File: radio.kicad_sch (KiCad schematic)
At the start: 28 parts, among them IC5 S2-LPQTR, IC6 BALF-SPI2-01D3, Y3 Crystal_GND24

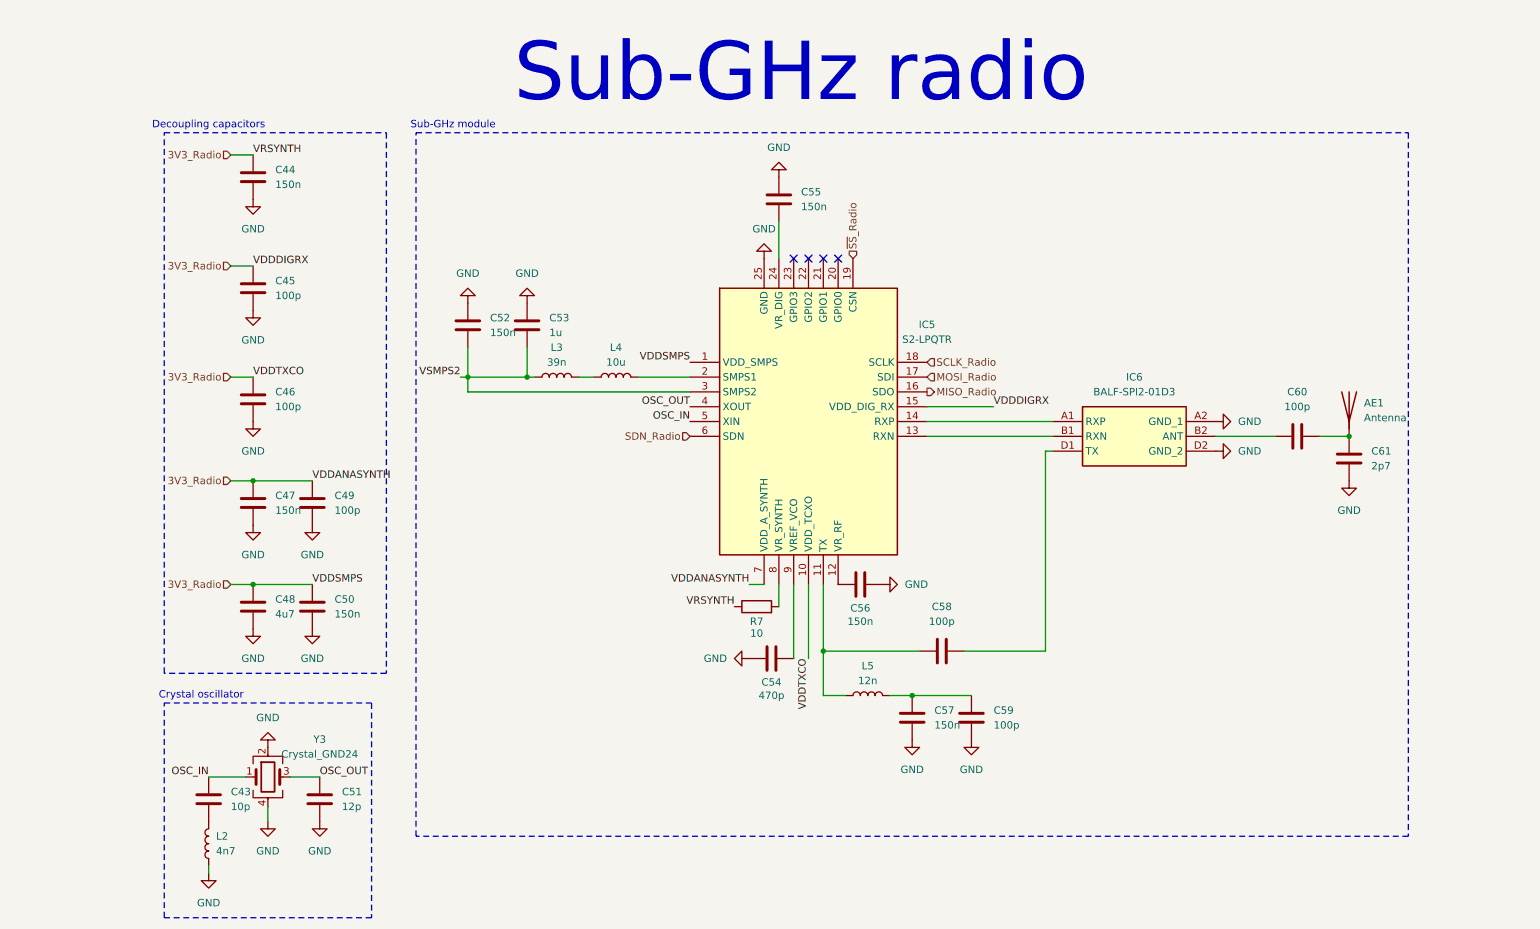
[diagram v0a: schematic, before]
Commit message: Setup crystal oscillators for MCU and S2LP
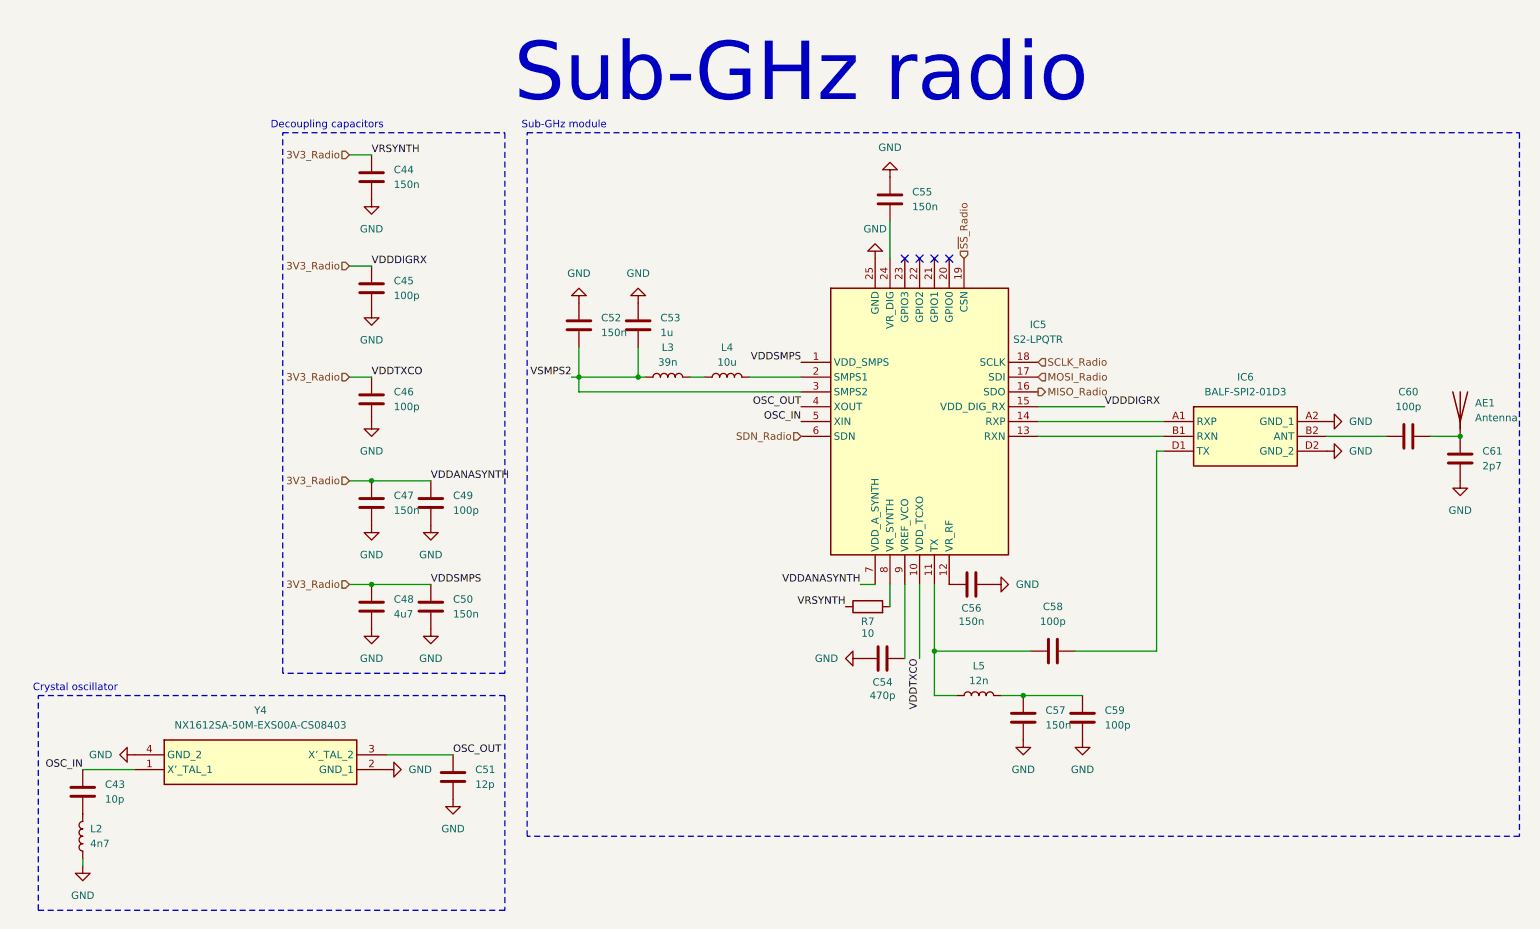
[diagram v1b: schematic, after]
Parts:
- removed Y3: Crystal_GND24, symbol Device:Crystal_GND24
- added Y4: NX1612SA-50M-EXS00A-CS08403, weather-station-poc-fp:NX1612SA50MEXS00ACS08403, symbol weather-station-poc-sym:NX1612SA-50M-EXS00A-CS08403
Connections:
- net GND: now also Y4.2 (GND_1), Y4.4 (GND_2)
- net OSC_IN: now also Y4.1 (X’_TAL_1)
- net OSC_OUT: now also Y4.3 (X’_TAL_2)
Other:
- moved on the sheet: AE1, C43, C44, C45, C46, C47, C48, C49, C50, C51, C52, C53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

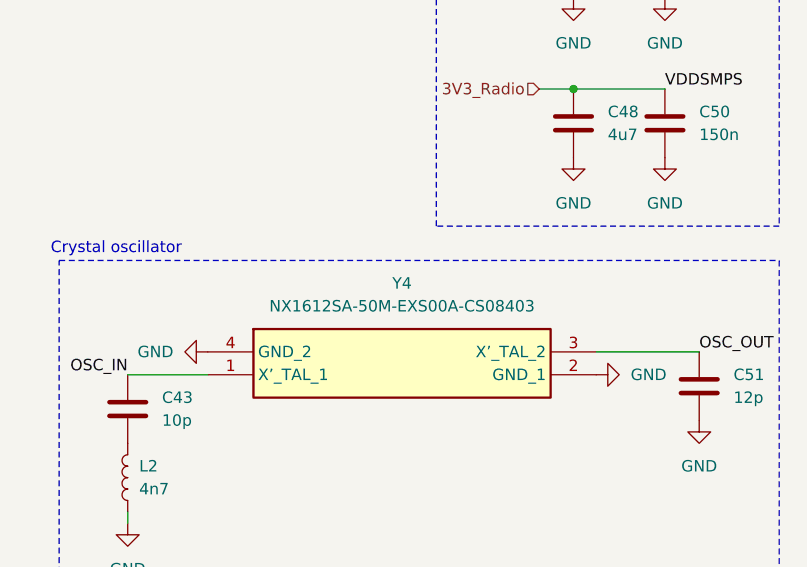
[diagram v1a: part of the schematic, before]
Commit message: Use preconised diodes for USB-C by ST
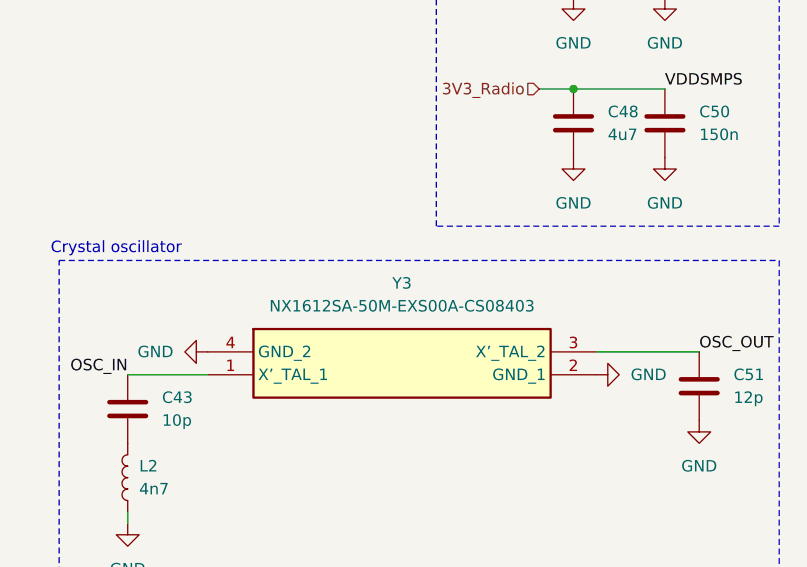
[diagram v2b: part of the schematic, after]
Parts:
- renumbered Y4 to Y3
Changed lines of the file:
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@@
 		(dnp no)
 		(fields_autoplaced yes)
-		(property "Reference" "#PWR077"
+		(property "Reference" "#PWR072"
 			(at 27.94 142.24 0)
 			(effects
@@
 			(project "weather-station-poc"
 				(path "/38eb53bb-294e-46e4-ad59-fd355ca373b9/31741ecc-719f-4191-b75e-d75152dfd251"
-					(reference "#PWR077")
+					(reference "#PWR072")
 					(unit 1)
 				)
@@
 		(dnp no)
 		(fields_autoplaced yes)
-		(property "Reference" "#PWR073"
+		(property "Reference" "#PWR074"
 			(at 74.93 72.39 0)
 			(effects
@@
 			(project "weather-station-poc"
 				(path "/38eb53bb-294e-46e4-ad59-fd355ca373b9/31741ecc-719f-4191-b75e-d75152dfd251"
-					(reference "#PWR073")
+					(reference "#PWR074")
 					(unit 1)
 				)
@@
 		(dnp no)
 		(fields_autoplaced yes)
-		(property "Reference" "Y4"
+		(property "Reference" "Y3"
 			(at 55.88 134.62 0)
 			(effects
@@
 			(project ""
 				(path "/38eb53bb-294e-46e4-ad59-fd355ca373b9/31741ecc-719f-4191-b75e-d75152dfd251"
-					(reference "Y4")
+					(reference "Y3")
 					(unit 1)
 				)
@@
 		(dnp no)
 		(fields_autoplaced yes)
-		(property "Reference" "#PWR075"
+		(property "Reference" "#PWR076"
 			(at 74.93 109.22 0)
 			(effects
@@
 			(project "weather-station-poc"
 				(path "/38eb53bb-294e-46e4-ad59-fd355ca373b9/31741ecc-719f-4191-b75e-d75152dfd251"
-					(reference "#PWR075")
+					(reference "#PWR076")
 					(unit 1)
 				)
@@
 		(dnp no)
 		(fields_autoplaced yes)
-		(property "Reference" "#PWR072"
+		(property "Reference" "#PWR073"
 			(at 74.93 53.34 0)
 			(effects
@@
 			(project "weather-station-poc"
 				(path "/38eb53bb-294e-46e4-ad59-fd355ca373b9/31741ecc-719f-4191-b75e-d75152dfd251"
-					(reference "#PWR072")
+					(reference "#PWR073")
 					(unit 1)
 				)
@@
 		(dnp no)
 		(fields_autoplaced yes)
-		(property "Reference" "#PWR076"
+		(property "Reference" "#PWR077"
 			(at 74.93 127 0)
 			(effects
@@
 			(project ""
 				(path "/38eb53bb-294e-46e4-ad59-fd355ca373b9/31741ecc-719f-4191-b75e-d75152dfd251"
-					(reference "#PWR076")
+					(reference "#PWR077")
 					(unit 1)
 				)
@@
 		(dnp no)
 		(fields_autoplaced yes)
-		(property "Reference" "#PWR074"
+		(property "Reference" "#PWR075"
 			(at 74.93 91.44 0)
 			(effects
@@
 			(project "weather-station-poc"
 				(path "/38eb53bb-294e-46e4-ad59-fd355ca373b9/31741ecc-719f-4191-b75e-d75152dfd251"
-					(reference "#PWR074")
+					(reference "#PWR075")
 					(unit 1)
 				)

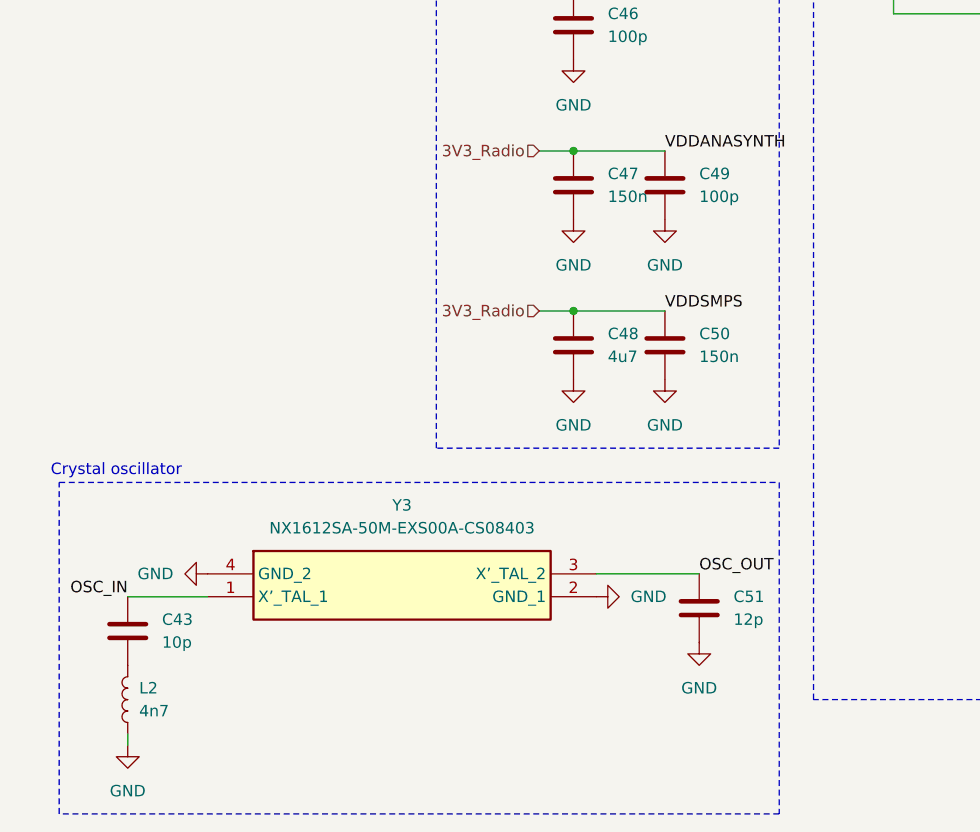
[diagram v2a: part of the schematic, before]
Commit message: Homogenation of symbols
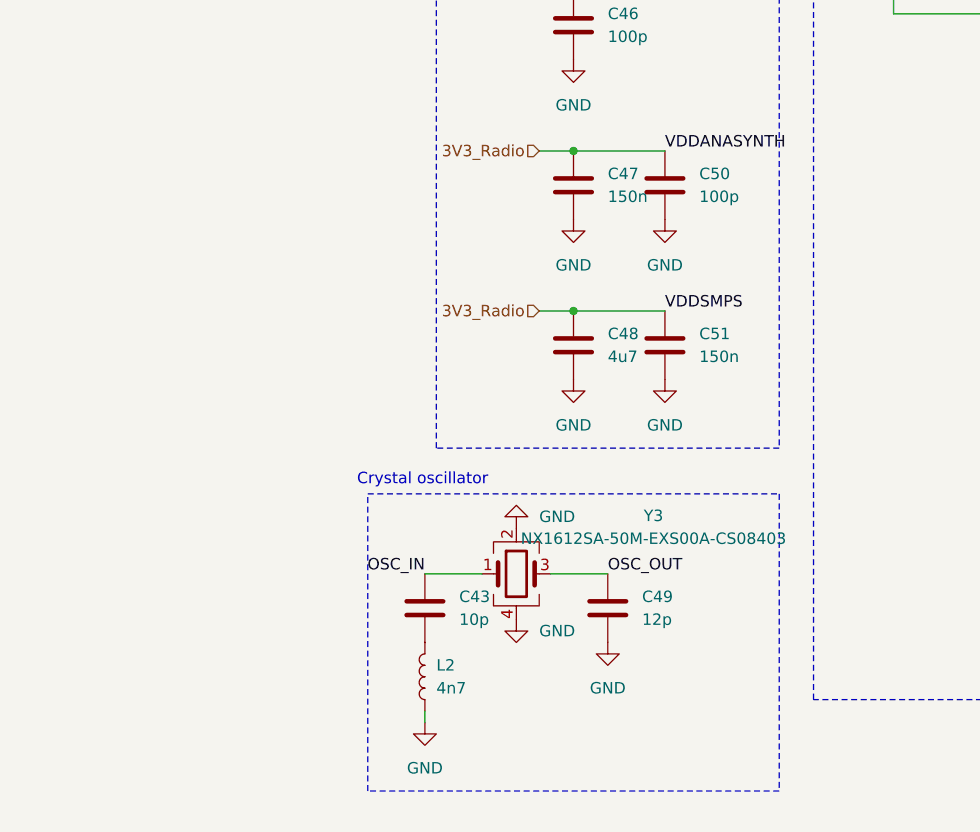
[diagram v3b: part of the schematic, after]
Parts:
- Y3: symbol weather-station-poc-sym:NX1612SA-50M-EXS00A-CS08403 -> Device:Crystal_GND24
- renumbered C51 to C49, C49 to C50, C50 to C51
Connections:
- net OSC_IN: now also C43.1; no longer C43.2
- net at L2.2: now also C43.2; no longer C43.1
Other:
- moved on the sheet: C43, C49, L2

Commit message: Fill the cartridge for all schematics
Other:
- company: (none) -> Julien Cruvieux
- title: (none) -> Radio Sub-GHz
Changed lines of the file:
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@@
 	(paper "A4")
 	(title_block
-		(date "2025-11-01")
+		(title "Radio Sub-GHz")
+		(date "2025-12-26")
+		(rev "A")
+		(company "Julien Cruvieux")
 	)
 	(rectangle
